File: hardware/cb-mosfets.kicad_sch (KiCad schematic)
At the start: 27 parts, among them Q901 Q_NMOS_GDS, Q902 Q_NMOS_GDS

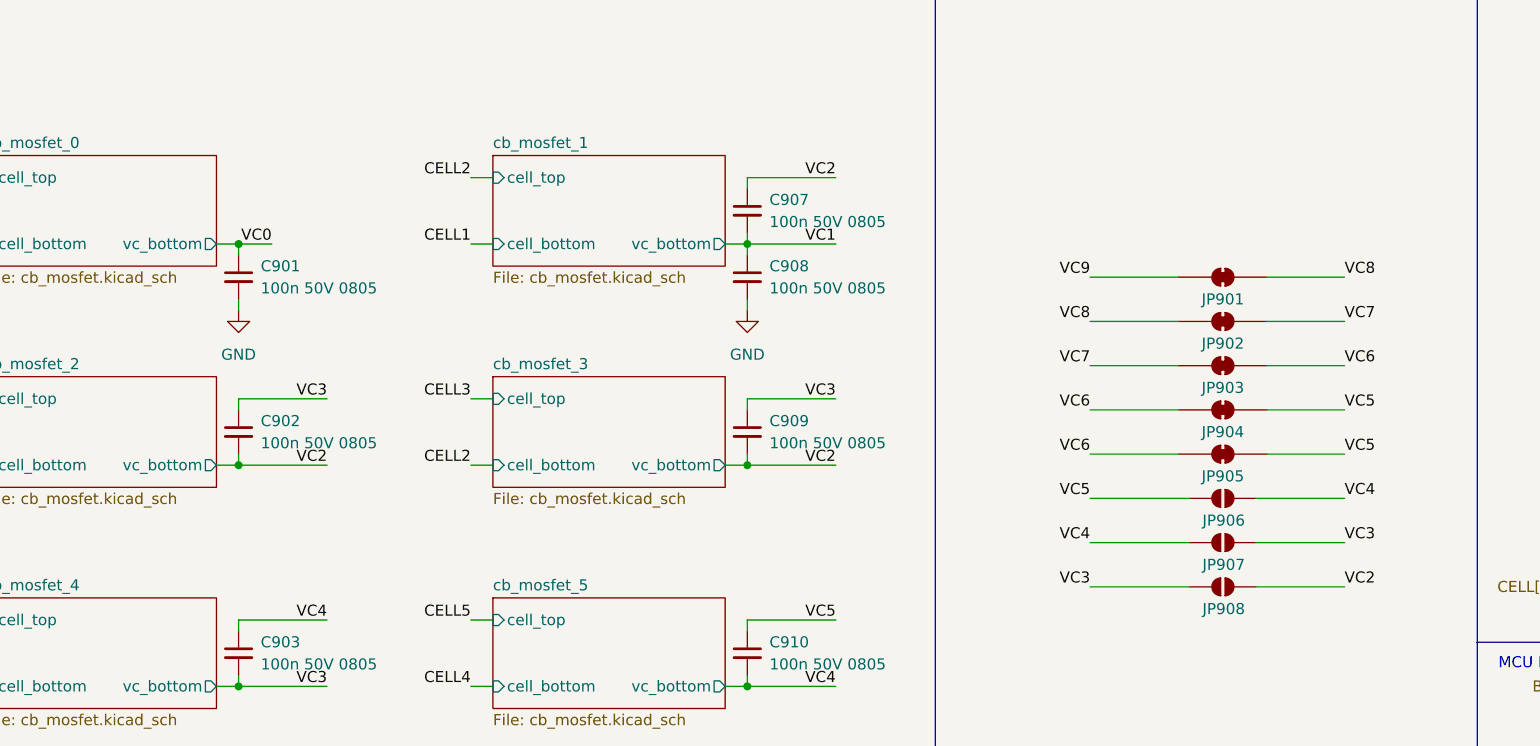
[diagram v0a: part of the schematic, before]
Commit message: simplify page
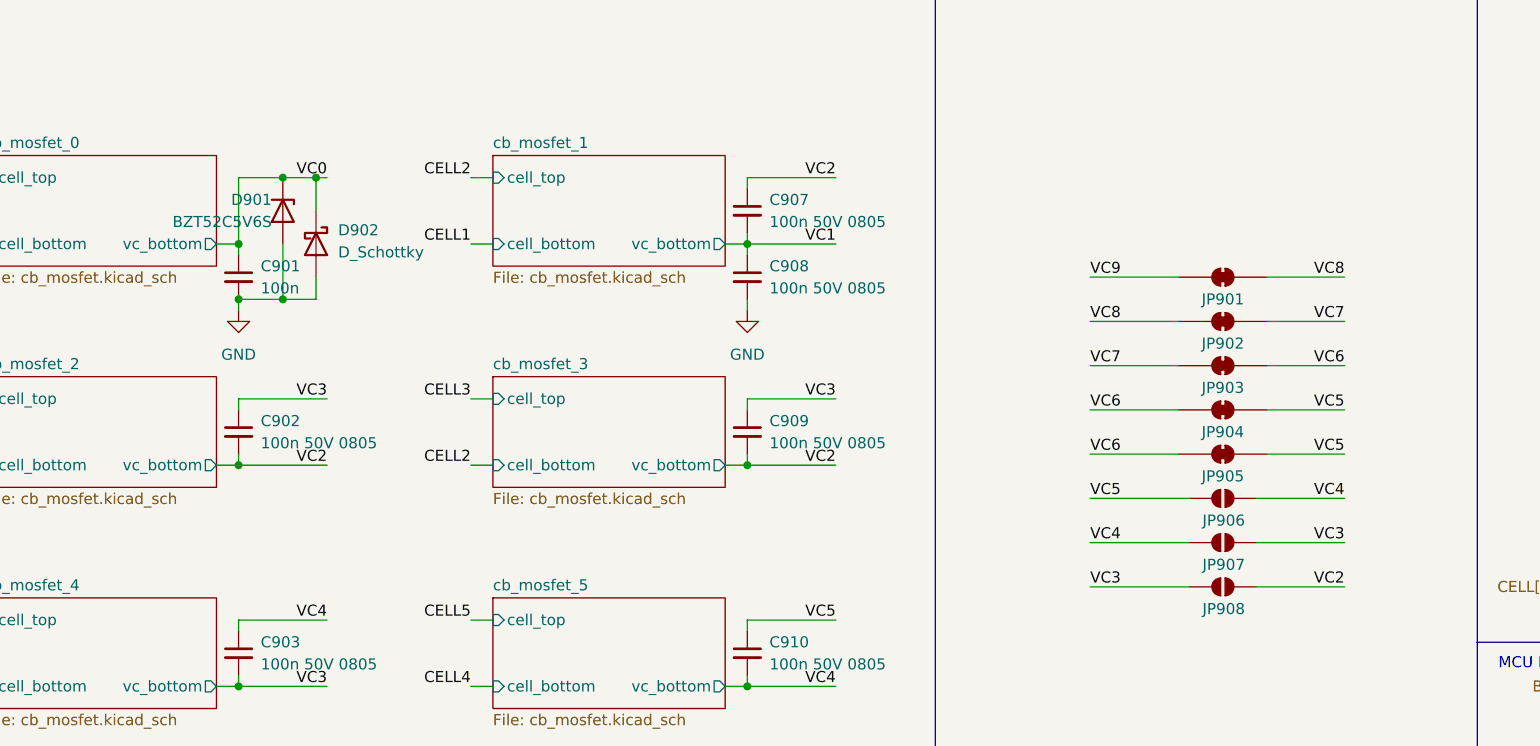
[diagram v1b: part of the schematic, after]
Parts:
- added D901: BZT52C5V6S, symbol Device:D_Zener
- added D902: D_Schottky, symbol Device:D_Schottky
- C901: value 100n 50V 0805 -> 100n
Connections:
- net GND: now also D901.2 (A), D902.2 (A)
- net VC0: now also D901.1 (K), D902.1 (K)

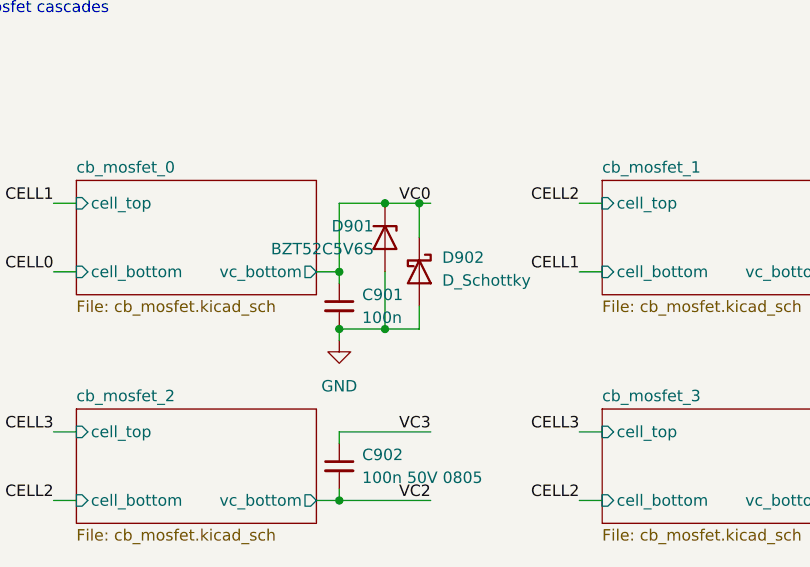
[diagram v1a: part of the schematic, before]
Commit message: simplify page
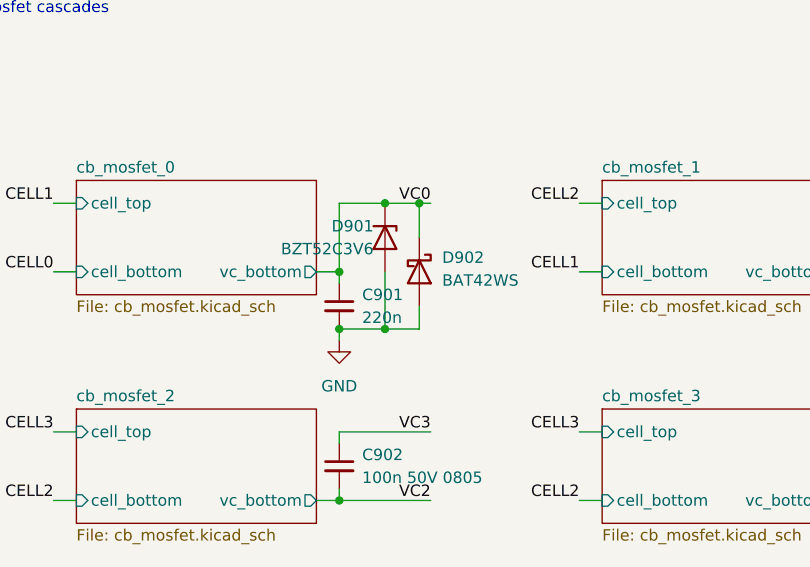
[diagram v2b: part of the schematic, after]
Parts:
- C901: value 100n -> 220n; LCSC C49678 -> C5378
- D901: value BZT52C5V6S -> BZT52C3V6; LCSC C19077441 -> C19077397
- D902: value D_Schottky -> BAT42WS; LCSC (none) -> C22466360

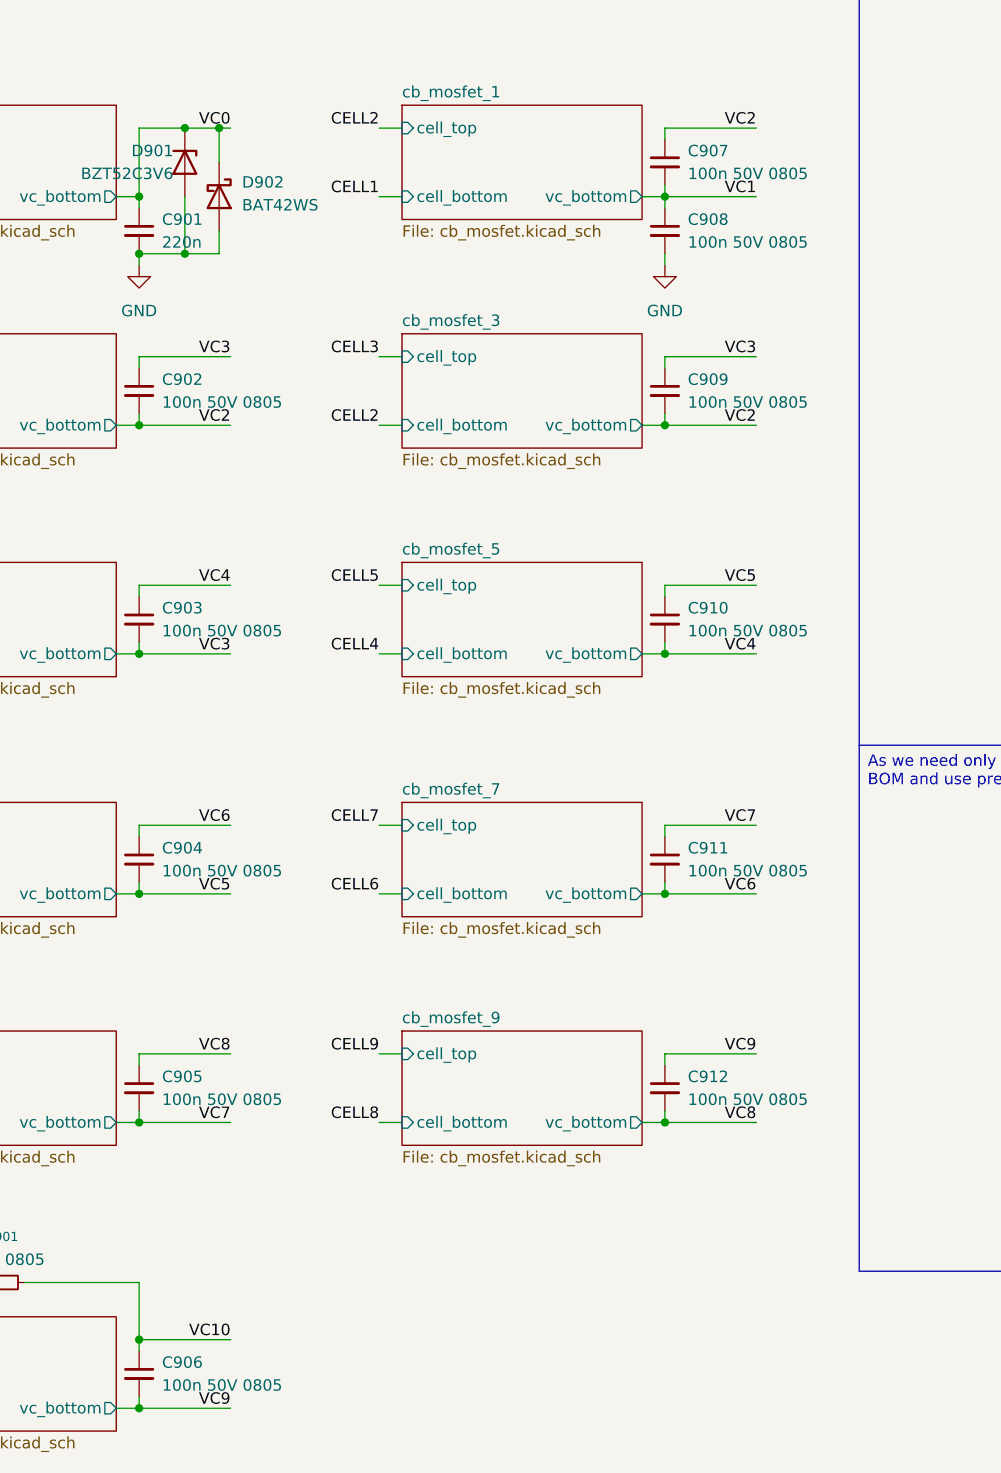
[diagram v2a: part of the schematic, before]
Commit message: switch capasitors to 220mf
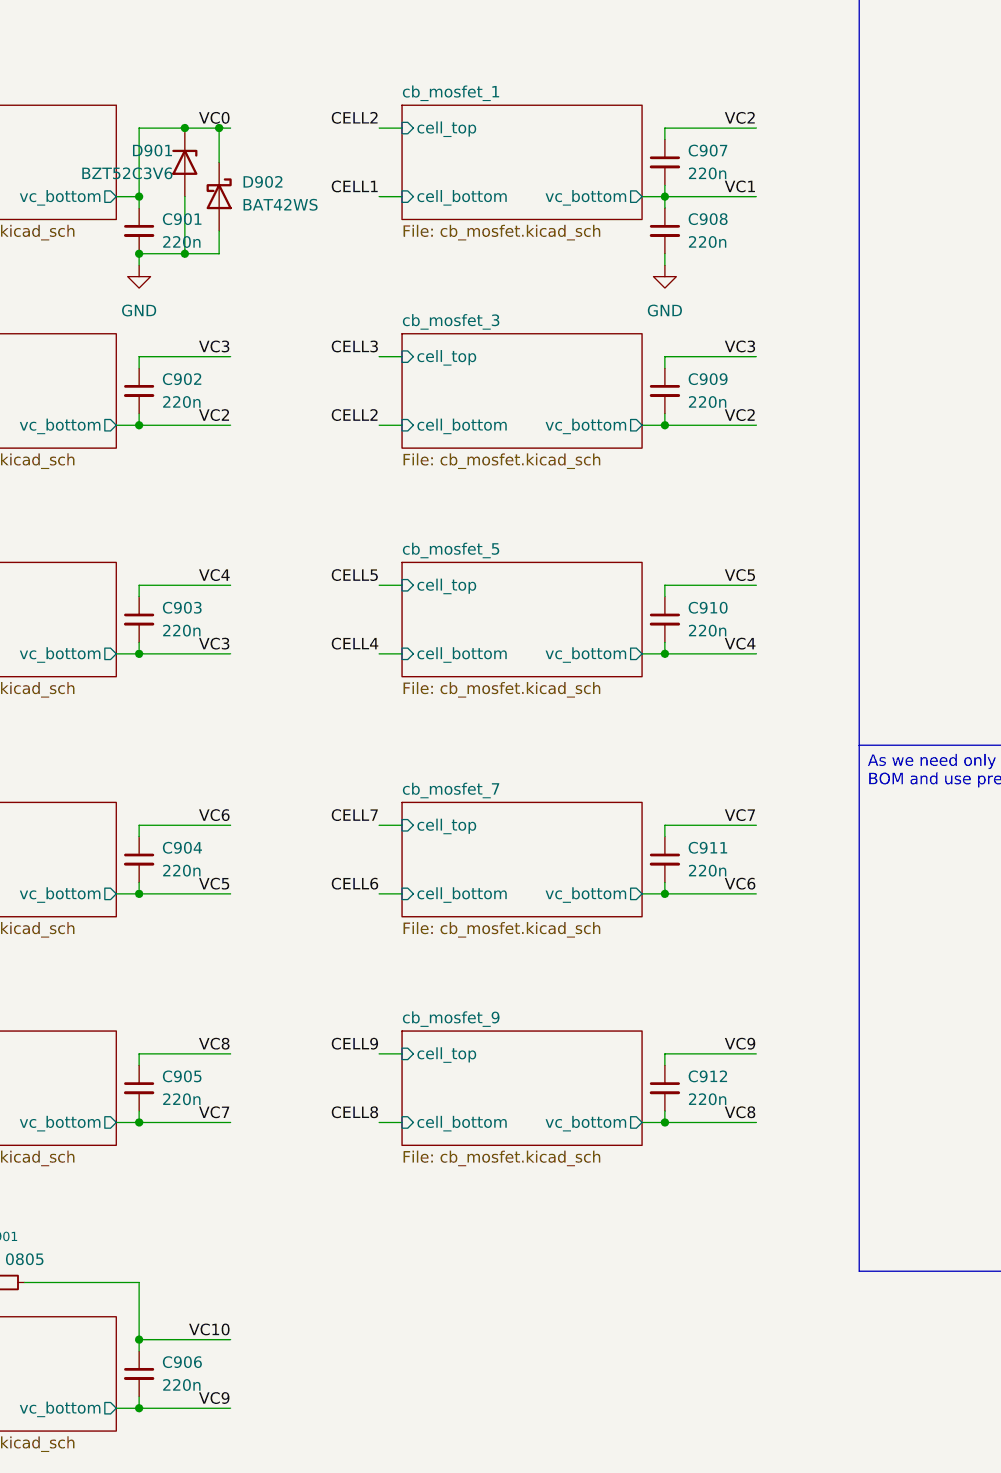
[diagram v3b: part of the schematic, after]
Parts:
- C902, C903, C904, C905, C906, C907, C908, C909, C910, C911, C912: value 100n 50V 0805 -> 220n; LCSC C49678 -> C5378

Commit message: x
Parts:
- C901, C902, C903, C904, C905, C906, C907, C908, C909, C910, C911, C912: footprint (none) -> Capacitor_SMD:C_0805_2012Metric
- D901: footprint (none) -> Diode_SMD:D_SOD-123
- R901, R902, R903, R904, R905: value 100R 0805 -> 100; footprint (none) -> Resistor_SMD:R_0805_2012Metric
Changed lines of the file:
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@@
 			)
 		)
-		(property "Value" "100R 0805"
+		(property "Value" "100"
 			(at 254 129.54 0)
 			(show_name no)
@@
 			)
 		)
-		(property "Footprint" ""
+		(property "Footprint" "Resistor_SMD:R_0805_2012Metric"
 			(at 246.38 128.27 0)
 			(hide yes)
@@
 			)
 		)
-		(property "Value" "100R 0805"
+		(property "Value" "100"
 			(at 215.9 132.08 0)
 			(show_name no)
@@
 			)
 		)
-		(property "Footprint" ""
+		(property "Footprint" "Resistor_SMD:R_0805_2012Metric"
 			(at 223.52 130.81 0)
 			(hide yes)
@@
 			)
 		)
-		(property "Footprint" ""
+		(property "Footprint" "Capacitor_SMD:C_0805_2012Metric"
 			(at 58.42 119.38 0)
 			(hide yes)
@@
 			)
 		)
-		(property "Footprint" ""
+		(property "Footprint" "Capacitor_SMD:C_0805_2012Metric"
 			(at 58.42 49.53 0)
 			(hide yes)
@@
 			)
 		)
-		(property "Footprint" ""
+		(property "Footprint" "Capacitor_SMD:C_0805_2012Metric"
 			(at 116.84 119.38 0)
 			(hide yes)
@@
 			)
 		)
-		(property "Footprint" ""
+		(property "Footprint" "Capacitor_SMD:C_0805_2012Metric"
 			(at 58.42 144.78 0)
 			(hide yes)
@@
 			)
 		)
-		(property "Footprint" ""
+		(property "Footprint" "Capacitor_SMD:C_0805_2012Metric"
 			(at 58.42 176.53 0)
 			(hide yes)
@@
 			)
 		)
-		(property "Value" "100R 0805"
+		(property "Value" "100"
 			(at 215.9 140.97 0)
 			(show_name no)
@@
 			)
 		)
-		(property "Footprint" ""
+		(property "Footprint" "Resistor_SMD:R_0805_2012Metric"
 			(at 223.52 139.7 0)
 			(hide yes)
@@
 			)
 		)
-		(property "Footprint" ""
+		(property "Footprint" "Capacitor_SMD:C_0805_2012Metric"
 			(at 116.84 144.78 0)
 			(hide yes)
@@
 			)
 		)
-		(property "Footprint" ""
+		(property "Footprint" "Capacitor_SMD:C_0805_2012Metric"
 			(at 116.84 92.71 0)
 			(hide yes)
@@
 			)
 		)
-		(property "Footprint" ""
+		(property "Footprint" "Capacitor_SMD:C_0805_2012Metric"
 			(at 58.42 92.71 0)
 			(hide yes)
@@
 			)
 		)
-		(property "Footprint" ""
+		(property "Footprint" "Diode_SMD:D_SOD-123"
 			(at 63.5 41.91 0)
 			(hide yes)
@@
 			)
 		)
-		(property "Footprint" ""
+		(property "Footprint" "Capacitor_SMD:C_0805_2012Metric"
 			(at 58.42 67.31 0)
 			(hide yes)
@@
 			)
 		)
-		(property "Footprint" ""
+		(property "Footprint" "Capacitor_SMD:C_0805_2012Metric"
 			(at 116.84 49.53 0)
 			(hide yes)
@@
 			)
 		)
-		(property "Footprint" ""
+		(property "Footprint" "Capacitor_SMD:C_0805_2012Metric"
 			(at 116.84 67.31 0)
 			(hide yes)
@@
 			)
 		)
-		(property "Value" "100R 0805"
+		(property "Value" "100"
 			(at 43.18 163.83 90)
 			(show_name no)
@@
 			)
 		)
-		(property "Footprint" ""
+		(property "Footprint" "Resistor_SMD:R_0805_2012Metric"
 			(at 43.18 166.37 0)
 			(hide yes)
@@
 			)
 		)
-		(property "Footprint" ""
+		(property "Footprint" "Capacitor_SMD:C_0805_2012Metric"
 			(at 116.84 41.91 0)
 			(hide yes)
@@
 			)
 		)
-		(property "Value" "100R 0805"
+		(property "Value" "100"
 			(at 254 118.11 0)
 			(show_name no)
@@
 			)
 		)
-		(property "Footprint" ""
+		(property "Footprint" "Resistor_SMD:R_0805_2012Metric"
 			(at 246.38 116.84 0)
 			(hide yes)
